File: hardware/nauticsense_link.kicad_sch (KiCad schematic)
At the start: 7 parts, among them J1 NMEA2000, J2 NMEA0183, U1 ESP32 DevKit, U2 SN65HVD230 CAN, U3 MAX490 RS-422

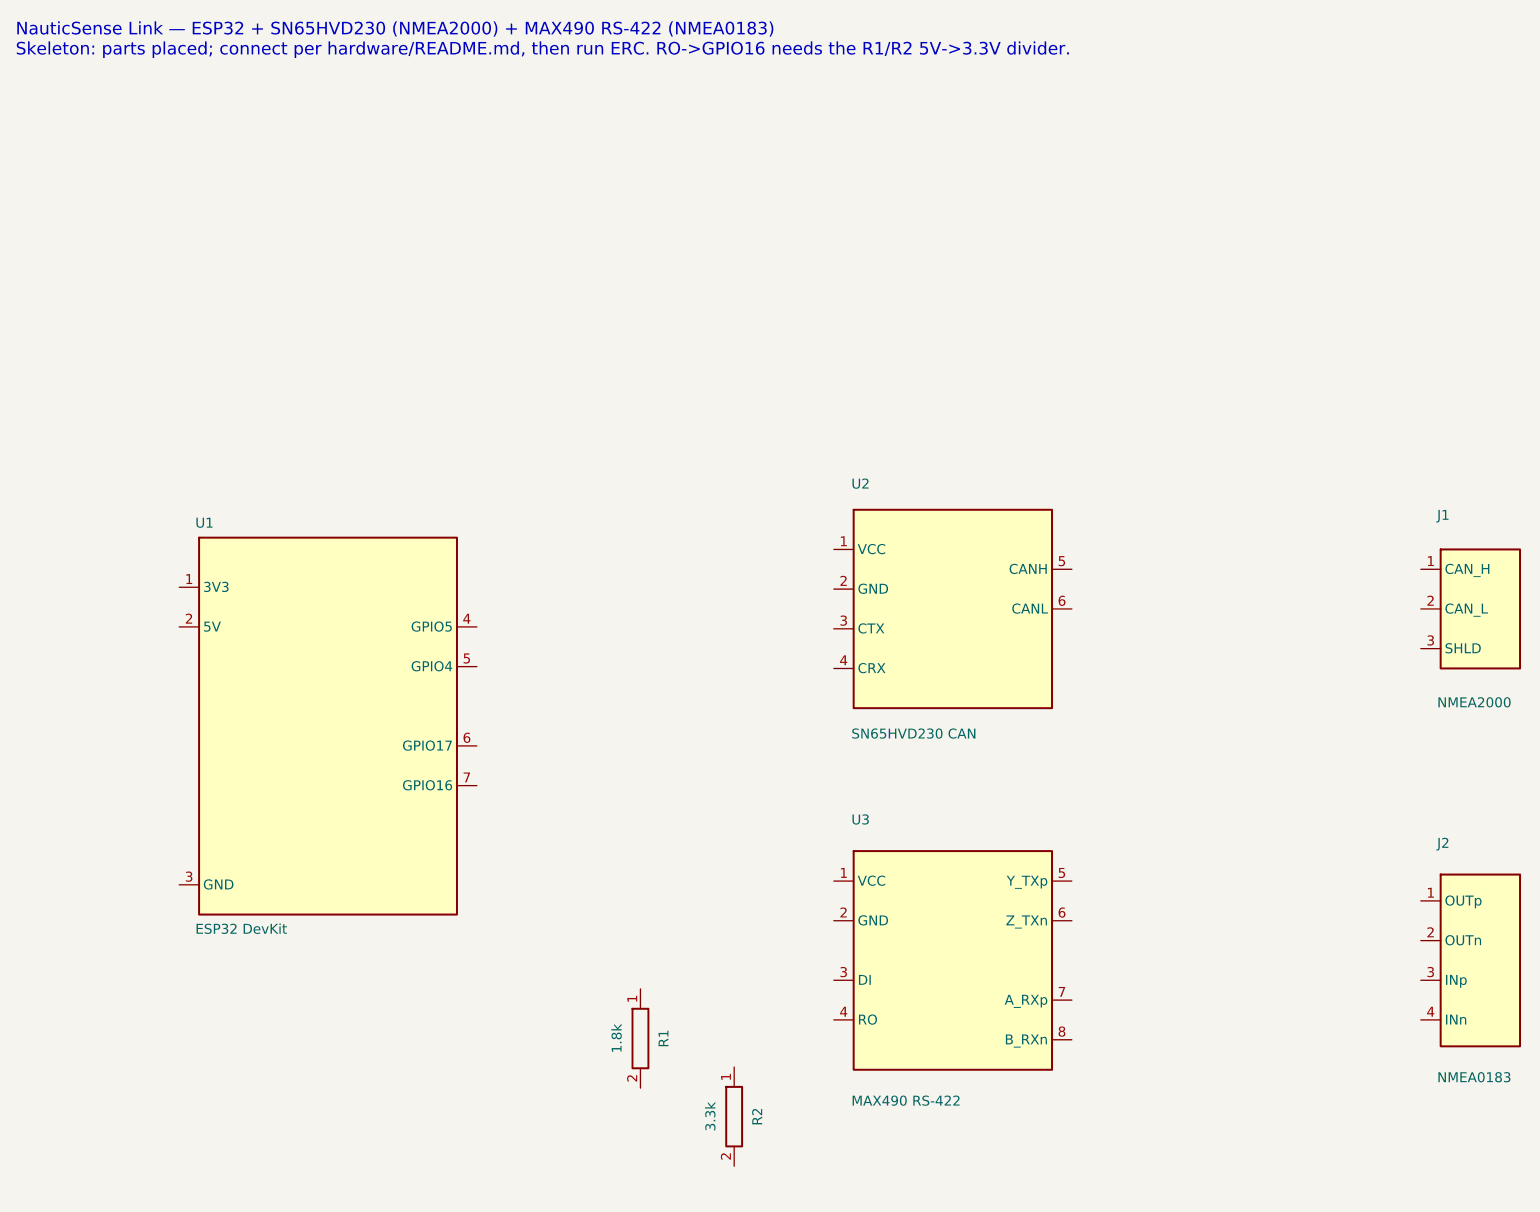
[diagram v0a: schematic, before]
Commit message: hardware: wire the KiCad schematic (global labels, net-by-name)
Add 32 wire stubs + 32 global labels connecting every pin to its net
(CAN_TX/CAN_RX, CAN_H/CAN_L, NMEA0183_TX, RO_5V->R1->NMEA0183_RX divider->R2->GND,
N0183 TX/RX pairs, +3V3/+5V/GND). The .kicad_sch now opens fully connected.

Co-Authored-By: Claude Opus 4.8 <noreply@anthropic.com>
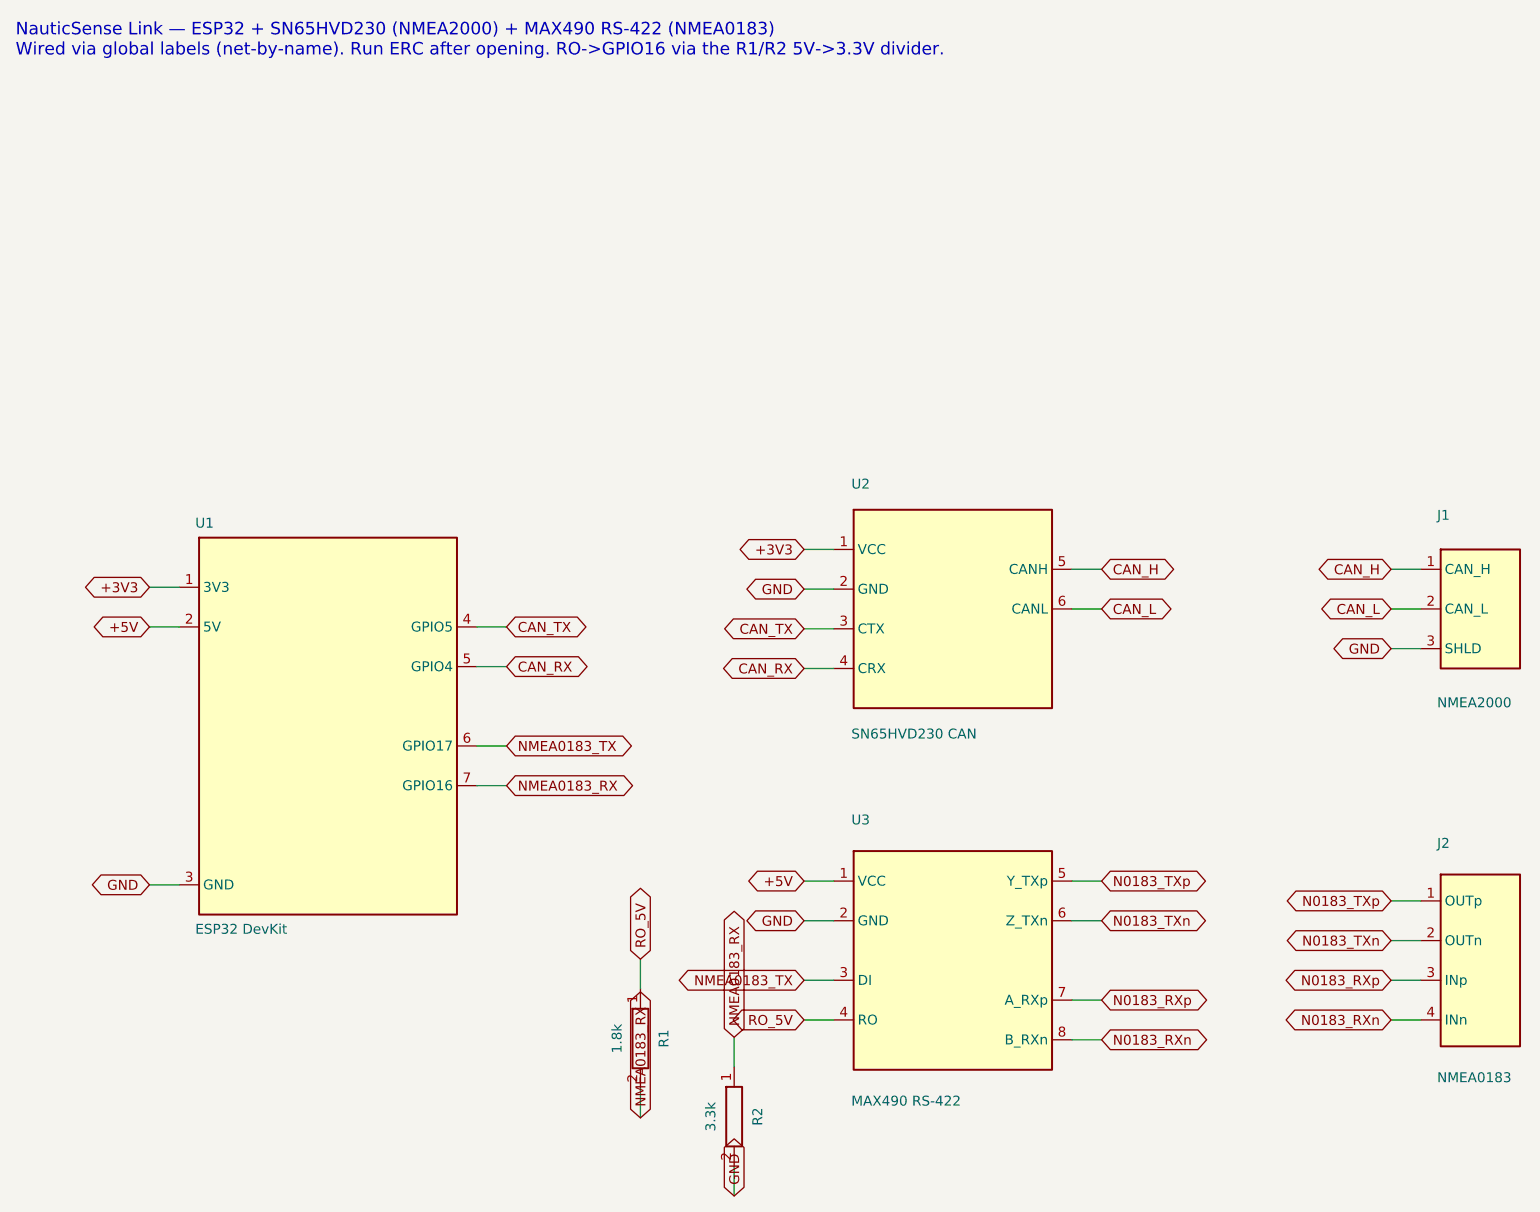
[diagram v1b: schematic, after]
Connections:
- net +3V3: now reaches U1.1 (3V3)
- net +3V3: now also U2.1 (VCC)
- net +5V: now reaches U1.2 (5V)
- net +5V: now also U3.1 (VCC)
- net GND: now reaches U1.3 (GND)
- net GND: now also J1.3 (SHLD), R2.2, U2.2 (GND), U3.2 (GND)
- net CAN_TX: now reaches U1.4 (GPIO5)
- net CAN_TX: now also U2.3 (CTX)
- net CAN_RX: now reaches U1.5 (GPIO4)
- net CAN_RX: now also U2.4 (CRX)
- net NMEA0183_TX: now reaches U1.6 (GPIO17)
- net NMEA0183_TX: now also U3.3 (DI)
- net NMEA0183_RX: now reaches U1.7 (GPIO16)
- net NMEA0183_RX: now also R1.2, R2.1
- net CAN_H: now reaches U2.5 (CANH)
- net CAN_H: now also J1.1 (CAN_H)
- net CAN_L: now reaches U2.6 (CANL)
- net CAN_L: now also J1.2 (CAN_L)
- net RO_5V: now reaches U3.4 (RO)
- net RO_5V: now also R1.1
- net N0183_TXp: now reaches U3.5 (Y_TXp)
- net N0183_TXp: now also J2.1 (OUTp)
- net N0183_TXn: now reaches U3.6 (Z_TXn)
- net N0183_TXn: now also J2.2 (OUTn)
- net N0183_RXp: now reaches U3.7 (A_RXp)
- net N0183_RXp: now also J2.3 (INp)
- net N0183_RXn: now reaches U3.8 (B_RXn)
- net N0183_RXn: now also J2.4 (INn)
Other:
- note added: "NauticSense Link — ESP32 + SN65HVD230 (NMEA2000) + MAX490 RS-422 (NMEA0183) Wired via global labels (net-by-name). Run ERC after opening. RO->GPIO16 via the R1/R2 5V->3.3V divider."
- note removed: "NauticSense Link — ESP32 + SN65HVD230 (NMEA2000) + MAX490 RS-422 (NMEA0183) Skeleton: parts placed; connect per hardware/README.md, then run ERC. RO->GPIO16 needs the R1/R2 5V->3.3V divider."
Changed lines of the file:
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@@
   (generator "nauticsense")
   (paper "A4")
-  (text "NauticSense Link — ESP32 + SN65HVD230 (NMEA2000) + MAX490 RS-422 (NMEA0183)\nSkeleton: parts placed; connect per hardware/README.md, then run ERC. RO->GPIO16 needs the R1/R2 5V->3.3V divider."
+  (text "NauticSense Link — ESP32 + SN65HVD230 (NMEA2000) + MAX490 RS-422 (NMEA0183)\nWired via global labels (net-by-name). Run ERC after opening. RO->GPIO16 via the R1/R2 5V->3.3V divider."
     (at 30 20 0) (effects (font (size 1.6 1.6)) (justify left top)))
   (symbol (lib_id "NauticSense:ESP32_DevKit") (at 70 110 0) (unit 1)
@@
     (instances (project "nauticsense" (path "/0a000000-0000-4000-8000-000000000001" (reference "R2") (unit 1))))
   )
+  (wire (pts (xy 50.95 92.22) (xy 47.14 92.22)) (stroke (width 0) (type default)))
+  (global_label "+3V3" (shape bidirectional) (at 47.14 92.22 180) (effects (font (size 1.27 1.27)) (justify right)))
+  (wire (pts (xy 50.95 97.30) (xy 47.14 97.30)) (stroke (width 0) (type default)))
+  (global_label "+5V" (shape bidirectional) (at 47.14 97.30 180) (effects (font (size 1.27 1.27)) (justify right)))
+  (wire (pts (xy 50.95 130.32) (xy 47.14 130.32)) (stroke (width 0) (type default)))
+  (global_label "GND" (shape bidirectional) (at 47.14 130.32 180) (effects (font (size 1.27 1.27)) (justify right)))
+  (wire (pts (xy 89.05 97.30) (xy 92.86 97.30)) (stroke (width 0) (type default)))
+  (global_label "CAN_TX" (shape bidirectional) (at 92.86 97.30 0) (effects (font (size 1.27 1.27)) (justify left)))
+  (wire (pts (xy 89.05 102.38) (xy 92.86 102.38)) (stroke (width 0) (type default)))
+  (global_label "CAN_RX" (shape bidirectional) (at 92.86 102.38 0) (effects (font (size 1.27 1.27)) (justify left)))
+  (wire (pts (xy 89.05 112.54) (xy 92.86 112.54)) (stroke (width 0) (type default)))
+  (global_label "NMEA0183_TX" (shape bidirectional) (at 92.86 112.54 0) (effects (font (size 1.27 1.27)) (justify left)))
+  (wire (pts (xy 89.05 117.62) (xy 92.86 117.62)) (stroke (width 0) (type default)))
+  (global_label "NMEA0183_RX" (shape bidirectional) (at 92.86 117.62 0) (effects (font (size 1.27 1.27)) (justify left)))
+  (wire (pts (xy 134.76 87.38) (xy 130.95 87.38)) (stroke (width 0) (type default)))
+  (global_label "+3V3" (shape bidirectional) (at 130.95 87.38 180) (effects (font (size 1.27 1.27)) (justify right)))
+  (wire (pts (xy 134.76 92.46) (xy 130.95 92.46)) (stroke (width 0) (type default)))
+  (global_label "GND" (shape bidirectional) (at 130.95 92.46 180) (effects (font (size 1.27 1.27)) (justify right)))
+  (wire (pts (xy 134.76 97.54) (xy 130.95 97.54)) (stroke (width 0) (type default)))
+  (global_label "CAN_TX" (shape bidirectional) (at 130.95 97.54 180) (effects (font (size 1.27 1.27)) (justify right)))
+  (wire (pts (xy 134.76 102.62) (xy 130.95 102.62)) (stroke (width 0) (type default)))
+  (global_label "CAN_RX" (shape bidirectional) (at 130.95 102.62 180) (effects (font (size 1.27 1.27)) (justify right)))
+  (wire (pts (xy 165.24 89.92) (xy 169.05 89.92)) (stroke (width 0) (type default)))
+  (global_label "CAN_H" (shape bidirectional) (at 169.05 89.92 0) (effects (font (size 1.27 1.27)) (justify left)))
+  (wire (pts (xy 165.24 95.00) (xy 169.05 95.00)) (stroke (width 0) (type default)))
+  (global_label "CAN_L" (shape bidirectional) (at 169.05 95.00 0) (effects (font (size 1.27 1.27)) (justify left)))
+  (wire (pts (xy 134.76 129.84) (xy 130.95 129.84)) (stroke (width 0) (type default)))
+  (global_label "+5V" (shape bidirectional) (at 130.95 129.84 180) (effects (font (size 1.27 1.27)) (justify right)))
+  (wire (pts (xy 134.76 134.92) (xy 130.95 134.92)) (stroke (width 0) (type default)))
+  (global_label "GND" (shape bidirectional) (at 130.95 134.92 180) (effects (font (size 1.27 1.27)) (justify right)))
+  (wire (pts (xy 134.76 142.54) (xy 130.95 142.54)) (stroke (width 0) (type default)))
+  (global_label "NMEA0183_TX" (shape bidirectional) (at 130.95 142.54 180) (effects (font (size 1.27 1.27)) (justify right)))
+  (wire (pts (xy 134.76 147.62) (xy 130.95 147.62)) (stroke (width 0) (type default)))
+  (global_label "RO_5V" (shape bidirectional) (at 130.95 147.62 180) (effects (font (size 1.27 1.27)) (justify right)))
+  (wire (pts (xy 165.24 129.84) (xy 169.05 129.84)) (stroke (width 0) (type default)))
+  (global_label "N0183_TXp" (shape bidirectional) (at 169.05 129.84 0) (effects (font (size 1.27 1.27)) (justify left)))
+  (wire (pts (xy 165.24 134.92) (xy 169.05 134.92)) (stroke (width 0) (type default)))
+  (global_label "N0183_TXn" (shape bidirectional) (at 169.05 134.92 0) (effects (font (size 1.27 1.27)) (justify left)))
+  (wire (pts (xy 165.24 145.08) (xy 169.05 145.08)) (stroke (width 0) (type default)))
+  (global_label "N0183_RXp" (shape bidirectional) (at 169.05 145.08 0) (effects (font (size 1.27 1.27)) (justify left)))
+  (wire (pts (xy 165.24 150.16) (xy 169.05 150.16)) (stroke (width 0) (type default)))
+  (global_label "N0183_RXn" (shape bidirectional) (at 169.05 150.16 0) (effects (font (size 1.27 1.27)) (justify left)))
+  (wire (pts (xy 209.92 89.92) (xy 206.11 89.92)) (stroke (width 0) (type default)))
+  (global_label "CAN_H" (shape bidirectional) (at 206.11 89.92 180) (effects (font (size 1.27 1.27)) (justify right)))
+  (wire (pts (xy 209.92 95.00) (xy 206.11 95.00)) (stroke (width 0) (type default)))
+  (global_label "CAN_L" (shape bidirectional) (at 206.11 95.00 180) (effects (font (size 1.27 1.27)) (justify right)))
+  (wire (pts (xy 209.92 100.08) (xy 206.11 100.08)) (stroke (width 0) (type default)))
+  (global_label "GND" (shape bidirectional) (at 206.11 100.08 180) (effects (font (size 1.27 1.27)) (justify right)))
+  (wire (pts (xy 209.92 132.38) (xy 206.11 132.38)) (stroke (width 0) (type default)))
+  (global_label "N0183_TXp" (shape bidirectional) (at 206.11 132.38 180) (effects (font (size 1.27 1.27)) (justify right)))
+  (wire (pts (xy 209.92 137.46) (xy 206.11 137.46)) (stroke (width 0) (type default)))
+  (global_label "N0183_TXn" (shape bidirectional) (at 206.11 137.46 180) (effects (font (size 1.27 1.27)) (justify right)))
+  (wire (pts (xy 209.92 142.54) (xy 206.11 142.54)) (stroke (width 0) (type default)))
+  (global_label "N0183_RXp" (shape bidirectional) (at 206.11 142.54 180) (effects (font (size 1.27 1.27)) (justify right)))
+  (wire (pts (xy 209.92 147.62) (xy 206.11 147.62)) (stroke (width 0) (type default)))
+  (global_label "N0183_RXn" (shape bidirectional) (at 206.11 147.62 180) (effects (font (size 1.27 1.27)) (justify right)))
+  (wire (pts (xy 110.00 143.65) (xy 110.00 139.84)) (stroke (width 0) (type default)))
+  (global_label "RO_5V" (shape bidirectional) (at 110.00 139.84 90) (effects (font (size 1.27 1.27)) (justify left)))
+  (wire (pts (xy 110.00 156.35) (xy 110.00 160.16)) (stroke (width 0) (type default)))
+  (global_label "NMEA0183_RX" (shape bidirectional) (at 110.00 160.16 270) (effects (font (size 1.27 1.27)) (justify left)))
+  (wire (pts (xy 122.00 153.65) (xy 122.00 149.84)) (stroke (width 0) (type default)))
+  (global_label "NMEA0183_RX" (shape bidirectional) (at 122.00 149.84 90) (effects (font (size 1.27 1.27)) (justify left)))
+  (wire (pts (xy 122.00 166.35) (xy 122.00 170.16)) (stroke (width 0) (type default)))
+  (global_label "GND" (shape bidirectional) (at 122.00 170.16 270) (effects (font (size 1.27 1.27)) (justify left)))
   (sheet_instances
     (path "/" (page "1"))
